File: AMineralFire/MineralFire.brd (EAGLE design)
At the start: 114.9 x 77 mm, 61 parts, among them IC1 LM358, Q1 20MHz, Q2 20MHz, T1 200mA/40V, U1 328P, U2 328P, U3 7805

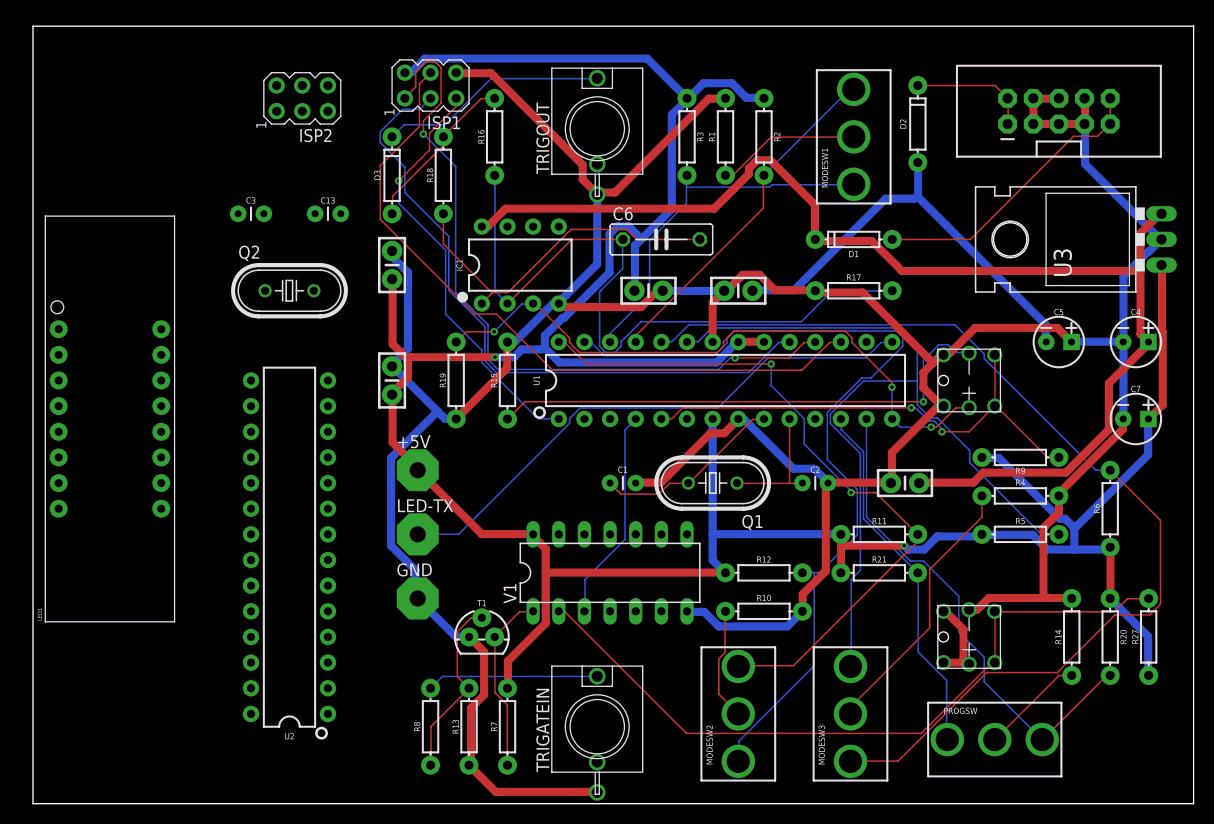
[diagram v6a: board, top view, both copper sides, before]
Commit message: adding Display
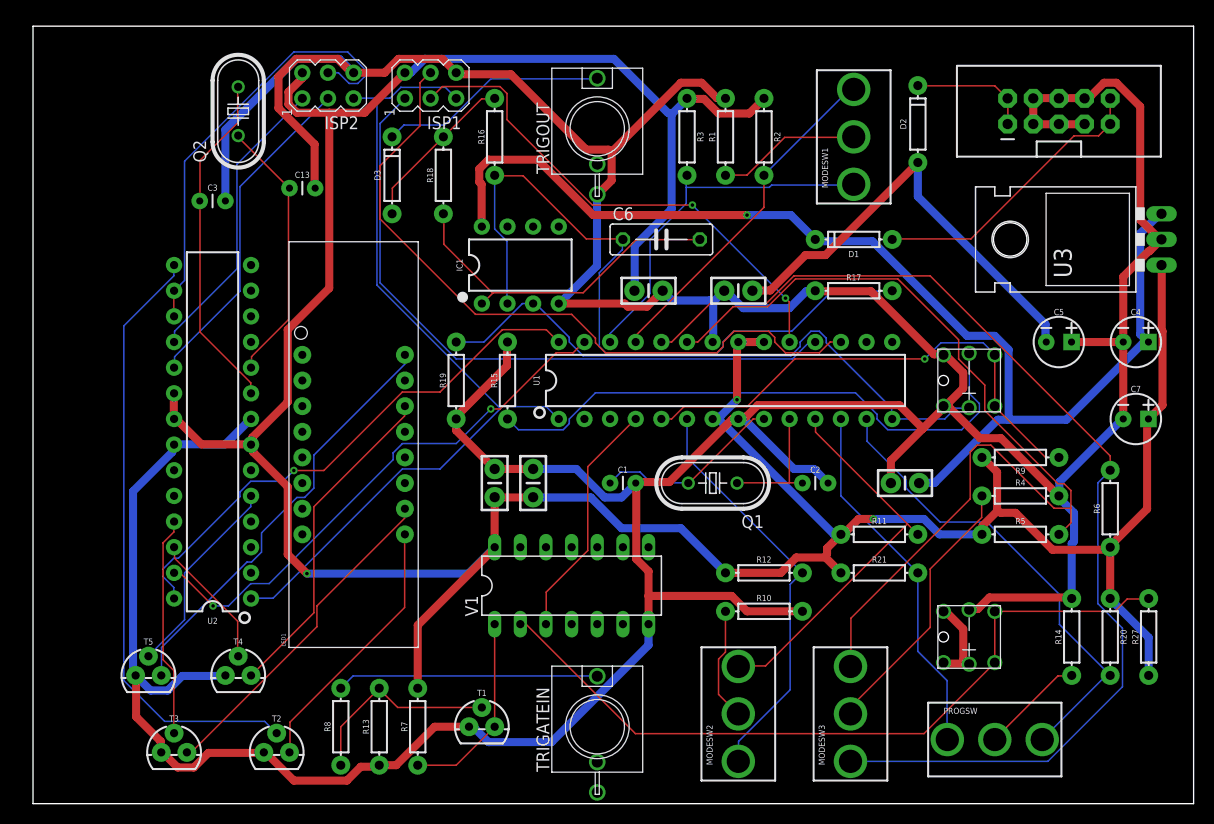
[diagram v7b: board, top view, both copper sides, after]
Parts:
- removed +5V, GND, LED-TX: WIREPAD4,16O1,6, wirepad:4,16O1,6
- added T2, T3, T4, T5: 200mA/40V, SparkFun-DiscreteSemi:TO-92
- moved LED1 24.3 mm to (31.8, 35.6)
- moved C11 23.9 mm to (45.7, 31.8)
- moved Q2 18.5 mm to (20.3, 68.6), turned to 90 degrees
- moved C12 17.3 mm to (49.5, 31.8)
- moved U2 13.7 mm to (17.8, 36.8)
- moved R13 8.89 mm to (34.3, 7.62)
- moved R7 8.89 mm to (38.1, 7.62)
- moved T1 8.89 mm to (44.5, 7.62)
- moved R8 8.89 mm to (30.5, 7.62)
- moved C3 4.02 mm to (17.8, 59.7)
- moved V1 4.02 mm to (53.3, 21.6)
- moved C13 3.59 mm to (26.7, 61.0)
- moved ISP2 2.84 mm to (29.2, 71.1)
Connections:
- removed net PR1: U1.11
- new net C-DIG1: T2.2, U2.15
- new net C-DIG2: T3.2, U2.25
- new net C-DIG3: T4.2, U2.26
- new net C-DIG4: T5.2, U2.5
- new net C-SECD: U2.12
- new net C-SEGA: U2.23
- new net C-SEGB: U2.4
- new net C-SEGC: U2.14
- new net C-SEGDP: U2.11
- new net C-SEGE: U2.13
- new net C-SEGF: U2.24
- new net C-SEGG: U2.6
- new net MISO2: ISP2.1, U2.18
- new net MOSI2: ISP2.4, U2.16, U2.17
- new net N$13: LED1.2, T3.3
- new net N$14: LED1.6, T4.3
- new net N$16: LED1.8, T5.3
- new net SCK2: ISP2.3, U2.19
- new net SCL: U1.28, U2.28
- new net SDA: U1.27, U2.27
- net +5V: no longer +5V.1
- net GND: now also T2.1, T3.1, T4.1, T5.1; no longer GND.1
- net MISO: no longer ISP2.1
- net MOSI: no longer ISP2.4
- net N$5: now also LED1.1, T2.3; no longer LED-TX.1, U1.15
- net SCK: no longer ISP2.3
- net T1: now also U1.11; no longer U1.28
- net T2: now also U1.6; no longer U1.27
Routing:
- net GND: track 362.2 -> 494.4 mm
- net C-DIG1: track 0.00 -> 60.5 mm
- net SDA: track 0.00 -> 53.2 mm, vias 0 -> 2
- net SCL: track 0.00 -> 53.2 mm, vias 0 -> 1
- net T2: track 86.9 -> 41.3 mm
- net MOSI2: track 0.00 -> 43.9 mm
- net RST: track 41.9 -> 85.7 mm, vias 1 -> 0
- net N$16: track 0.00 -> 42.5 mm
- net N$7: track 0.00 -> 34.0 mm
- net N$13: track 0.00 -> 33.3 mm
- net N$14: track 0.00 -> 33.0 mm
- net SCK2: track 0.00 -> 33.0 mm
- net T1: track 69.9 -> 38.3 mm, vias 2 -> 0
- net MISO2: track 0.00 -> 29.4 mm
- net N$5: track 55.2 -> 26.3 mm
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
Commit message: first layout
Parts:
- removed LED1: YSD-439AB4B-35, SparkFun-LED:7-SEGMENT-4DIGIT-YOUNGSUN
- added DS1: TDCG1060M, TDCG1060M:DIPS1016W50P254L4020H700Q16N
- added Q3, Q4, Q5, Q6, Q7, Q8, Q9: 2N3906, transistor-pnp:TO92
- added R22, R23, R24, R25, R26, R28, R29: 100, SparkFun-Resistors:AXIAL-0.3EZ
- moved C12 37.8 mm to (24.1, 59.7), turned to 180 degrees
- moved R19 10.5 mm to (44.5, 31.8)
- moved C11 6.35 mm to (52.1, 31.8)
- moved T5 6.35 mm to (17.8, 12.7)
- moved R16 4.02 mm to (47.0, 69.8)
- moved T3 3.81 mm to (17.8, 5.08)
- moved T4 3.81 mm to (24.1, 12.7)
- moved C3 3.59 mm to (15.2, 62.2)
- moved U2 2.84 mm to (20.3, 38.1)
- moved C13 2.54 mm to (26.7, 63.5)
- moved D3 1.80 mm to (34.3, 63.5)
- moved R18 1.27 mm to (41.9, 62.2)
- flipped BUT to the bottom
- flipped BUT1 to the bottom
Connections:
- removed net C-SECD: U2.12
- new net AN-A: DS1.14, R29.P$1
- new net AN-B: DS1.16, R24.P$1
- new net AN-C: DS1.13, R28.P$1
- new net AN-D: DS1.3, R23.P$1
- new net AN-E: DS1.5, R22.P$1
- new net AN-F: DS1.11, R26.P$1
- new net AN-G: DS1.15, R25.P$1
- new net C-SEGD: Q3.2, U2.12
- new net D1: DS1.1, T2.3
- new net D2: DS1.2, T3.3
- new net D3: DS1.6, T4.3
- new net D4: DS1.8, T5.3
- new net N$17: Q6.1, R25.P$2
- new net N$19: BUT1.K, R27.P$1
- new net N$20: Q5.1, R29.P$2
- net +5V: now also BUT1.1, BUT1.2, Q3.3, Q4.3, Q5.3, Q6.3, Q7.3, Q8.3, Q9.3; no longer R27.P$1
- net C-SEGA: now also Q5.2
- net C-SEGB: now also Q9.2
- net C-SEGC: now also Q7.2
- net C-SEGE: now also Q4.2
- net C-SEGF: now also Q8.2
- net C-SEGG: now also Q6.2
- net GND: now also R27.P$2; no longer BUT1.K
- net LBUTTON: now also BUT1.3, BUT1.4, BUT1.A; no longer BUT1.1, BUT1.2, R27.P$2
- net N$11: now also Q3.1, R23.P$2; no longer BUT1.3, BUT1.4, BUT1.A
- net N$13: now also Q9.1, R24.P$2; no longer LED1.2, T3.3
- net N$14: now also Q8.1, R26.P$2; no longer LED1.6, T4.3
- net N$16: now also Q7.1, R28.P$2; no longer LED1.8, T5.3
- net N$5: now also Q4.1, R22.P$2; no longer LED1.1, T2.3
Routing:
- net GND: track 494.4 -> 0.00 mm
- net +5V: track 331.9 -> 0.00 mm, vias 3 -> 0
- net +12V: track 115.8 -> 0.00 mm, vias 1 -> 0
- net T6: track 108.9 -> 0.00 mm
- net T5: track 95.7 -> 0.00 mm
- net RST: track 85.7 -> 0.00 mm
- net LBUTTON: track 75.3 -> 0.00 mm
- net N$32: track 72.3 -> 0.00 mm
- net MOSI: track 70.7 -> 0.00 mm
- net MISO: track 66.2 -> 0.00 mm
- net TRIGO: track 61.0 -> 0.00 mm
- net C-DIG1: track 60.5 -> 0.00 mm
- net N$31: track 57.7 -> 0.00 mm
- net SDA: track 53.2 -> 0.00 mm, vias 2 -> 0
- net SCL: track 53.2 -> 0.00 mm, vias 1 -> 0
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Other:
- board text added: "@R2Project. 2017 Designed by Andy C Hardware inspired by GMSN! ADSR Display based on SparkFun OpenSegment Serial Display"
- board text added: "Board_v0.2"
- board text removed: "@R2Project. Designed by Andy C Grateful to GMSN! for all their help!"
